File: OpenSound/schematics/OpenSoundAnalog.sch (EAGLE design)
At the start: 68 parts, among them IC1 MCP4822-E/PSOIC8, IC2 QUAD_OPAMPD, IC3 LM317MABT, Q601 BC846, Q701 BC846, Q801 BC846, Q903 BC846, U1 SN74LVC3G17DCTR

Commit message: part routed
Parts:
- added C5: 10u, rcl:CPOL-EUSANYO_SMD_A5
- C2: value 1u -> 10u
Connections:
- net +3V3: no longer C1.1
- net +5V: now also C1.1, C5.+
- net GND: now also C5.-
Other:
- moved on the sheet: C1
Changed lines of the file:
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@@
 <part name="C1" library="resistor" deviceset="C-EU" device="C0603" value="100nF"/>
 <part name="+3V2" library="supply1" deviceset="+3V3" device=""/>
-<part name="+3V3" library="supply1" deviceset="+3V3" device=""/>
 <part name="GND2" library="supply1" deviceset="GND" device=""/>
 <part name="GND3" library="supply1" deviceset="GND" device=""/>
@@
 <part name="P+1" library="supply1" deviceset="+12V" device=""/>
 <part name="P+5" library="supply1" deviceset="+5V" device=""/>
-<part name="C2" library="rcl" deviceset="CPOL-EU" device="SANYO_SMD_A5" value="1u"/>
+<part name="C2" library="rcl" deviceset="CPOL-EU" device="SANYO_SMD_A5" value="10u"/>
 <part name="P+8" library="supply1" deviceset="+5V" device=""/>
 <part name="U1" library="Rebel" deviceset="SN74LVC3G17DCTR" device=""/>
@@
 <part name="R101" library="Rebel" deviceset="R-EU_" device="0603" value="150R"/>
 <part name="C100" library="rcl" deviceset="C-EU" device="C0603" value="100n"/>
+<part name="P+6" library="supply1" deviceset="+5V" device=""/>
+<part name="C5" library="rcl" deviceset="CPOL-EU" device="SANYO_SMD_A5" value="10u"/>
+<part name="P+10" library="supply1" deviceset="+5V" device=""/>
+<part name="GND27" library="supply1" deviceset="GND" device=""/>
 </parts>
 <sheets>
@@
 <instance part="P-7" gate="1" x="157.48" y="30.48"/>
 <instance part="P+2" gate="1" x="157.48" y="50.8"/>
-<instance part="C1" gate="G$1" x="73.66" y="104.14"/>
+<instance part="C1" gate="G$1" x="127" y="-35.56"/>
 <instance part="+3V2" gate="G$1" x="66.04" y="114.3"/>
-<instance part="+3V3" gate="G$1" x="73.66" y="114.3"/>
 <instance part="GND2" gate="1" x="66.04" y="93.98"/>
-<instance part="GND3" gate="1" x="73.66" y="93.98"/>
+<instance part="GND3" gate="1" x="127" y="-45.72"/>
 <instance part="Q903" gate="G$1" x="-19.05" y="97.79"/>
 <instance part="R901" gate="G$1" x="-26.67" y="97.79" rot="MR180"/>
@@
 <instance part="R101" gate="G$1" x="226.06" y="167.64" rot="MR0"/>
 <instance part="C100" gate="G$1" x="223.52" y="154.94" rot="R180"/>
+<instance part="P+6" gate="1" x="127" y="-25.4"/>
+<instance part="C5" gate="G$1" x="55.88" y="104.14"/>
+<instance part="P+10" gate="1" x="55.88" y="114.3"/>
+<instance part="GND27" gate="1" x="55.88" y="93.98"/>
 </instances>
 <busses>
@@
 <pinref part="C1" gate="G$1" pin="2"/>
 <pinref part="GND3" gate="1" pin="GND"/>
-<wire x1="73.66" y1="96.52" x2="73.66" y2="99.06" width="0.1524" layer="91"/>
+<wire x1="127" y1="-43.18" x2="127" y2="-40.64" width="0.1524" layer="91"/>
 </segment>
 <segment>
@@
 <pinref part="C100" gate="G$1" pin="1"/>
 </segment>
+<segment>
+<pinref part="GND27" gate="1" pin="GND"/>
+<pinref part="C5" gate="G$1" pin="-"/>
+<wire x1="55.88" y1="96.52" x2="55.88" y2="99.06" width="0.1524" layer="91"/>
+</segment>
 </net>
 <net name="-12V" class="0">
@@
 <wire x1="101.6" y1="48.26" x2="104.14" y2="48.26" width="0.1524" layer="91"/>
 <wire x1="104.14" y1="48.26" x2="104.14" y2="53.34" width="0.1524" layer="91"/>
+</segment>
+<segment>
+<pinref part="C1" gate="G$1" pin="1"/>
+<wire x1="127" y1="-33.02" x2="127" y2="-27.94" width="0.1524" layer="91"/>
+<pinref part="P+6" gate="1" pin="+5V"/>
+</segment>
+<segment>
+<pinref part="C5" gate="G$1" pin="+"/>
+<pinref part="P+10" gate="1" pin="+5V"/>
+<wire x1="55.88" y1="106.68" x2="55.88" y2="111.76" width="0.1524" layer="91"/>
 </segment>
 </net>
@@
 </segment>
 <segment>
-<pinref part="+3V3" gate="G$1" pin="+3V3"/>
-<pinref part="C1" gate="G$1" pin="1"/>
-<wire x1="73.66" y1="106.68" x2="73.66" y2="111.76" width="0.1524" layer="91"/>
-</segment>
-<segment>

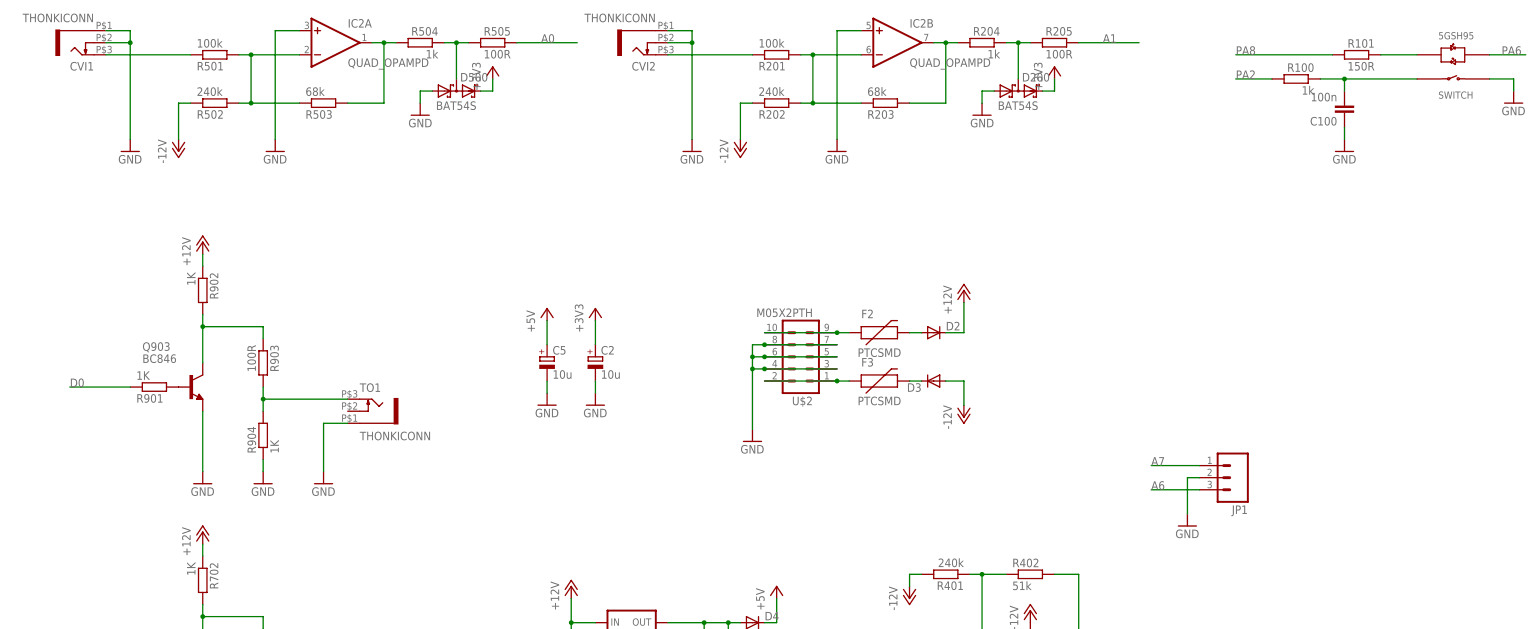
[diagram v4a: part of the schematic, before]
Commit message: connected button and completed routing
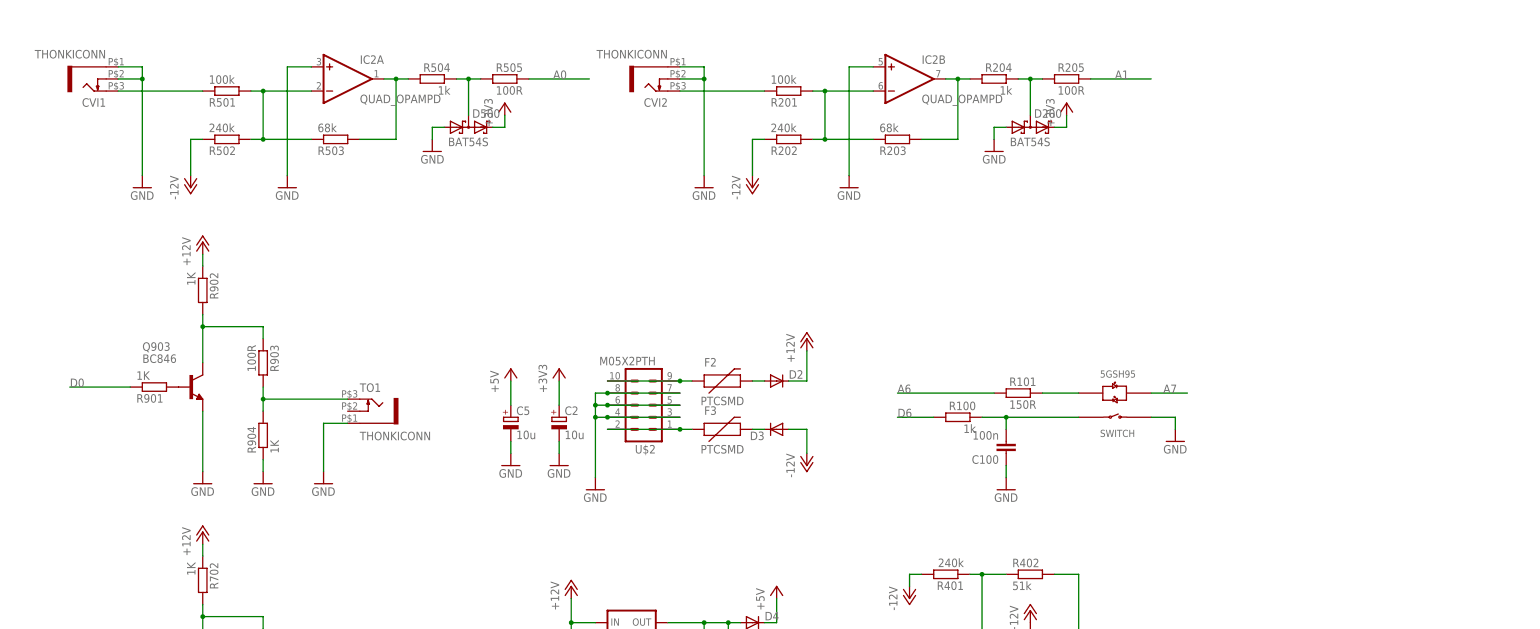
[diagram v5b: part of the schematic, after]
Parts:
- removed JP1: (no value), SparkFun-Connectors:M031X03_NO_SILK
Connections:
- removed net PA2: R100.2
- removed net PA6: U$1.LED_R+
- removed net PA8: R101.2
- net A6: now also R101.2; no longer JP1.3
- net A7: now also U$1.LED_R+; no longer JP1.1
- net D6: now also R100.2
- net GND: no longer JP1.2
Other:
- moved on the sheet: C100, C2, C5, CVI1, CVI2, D2, D200, D3, D500, F2, F3, IC2A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

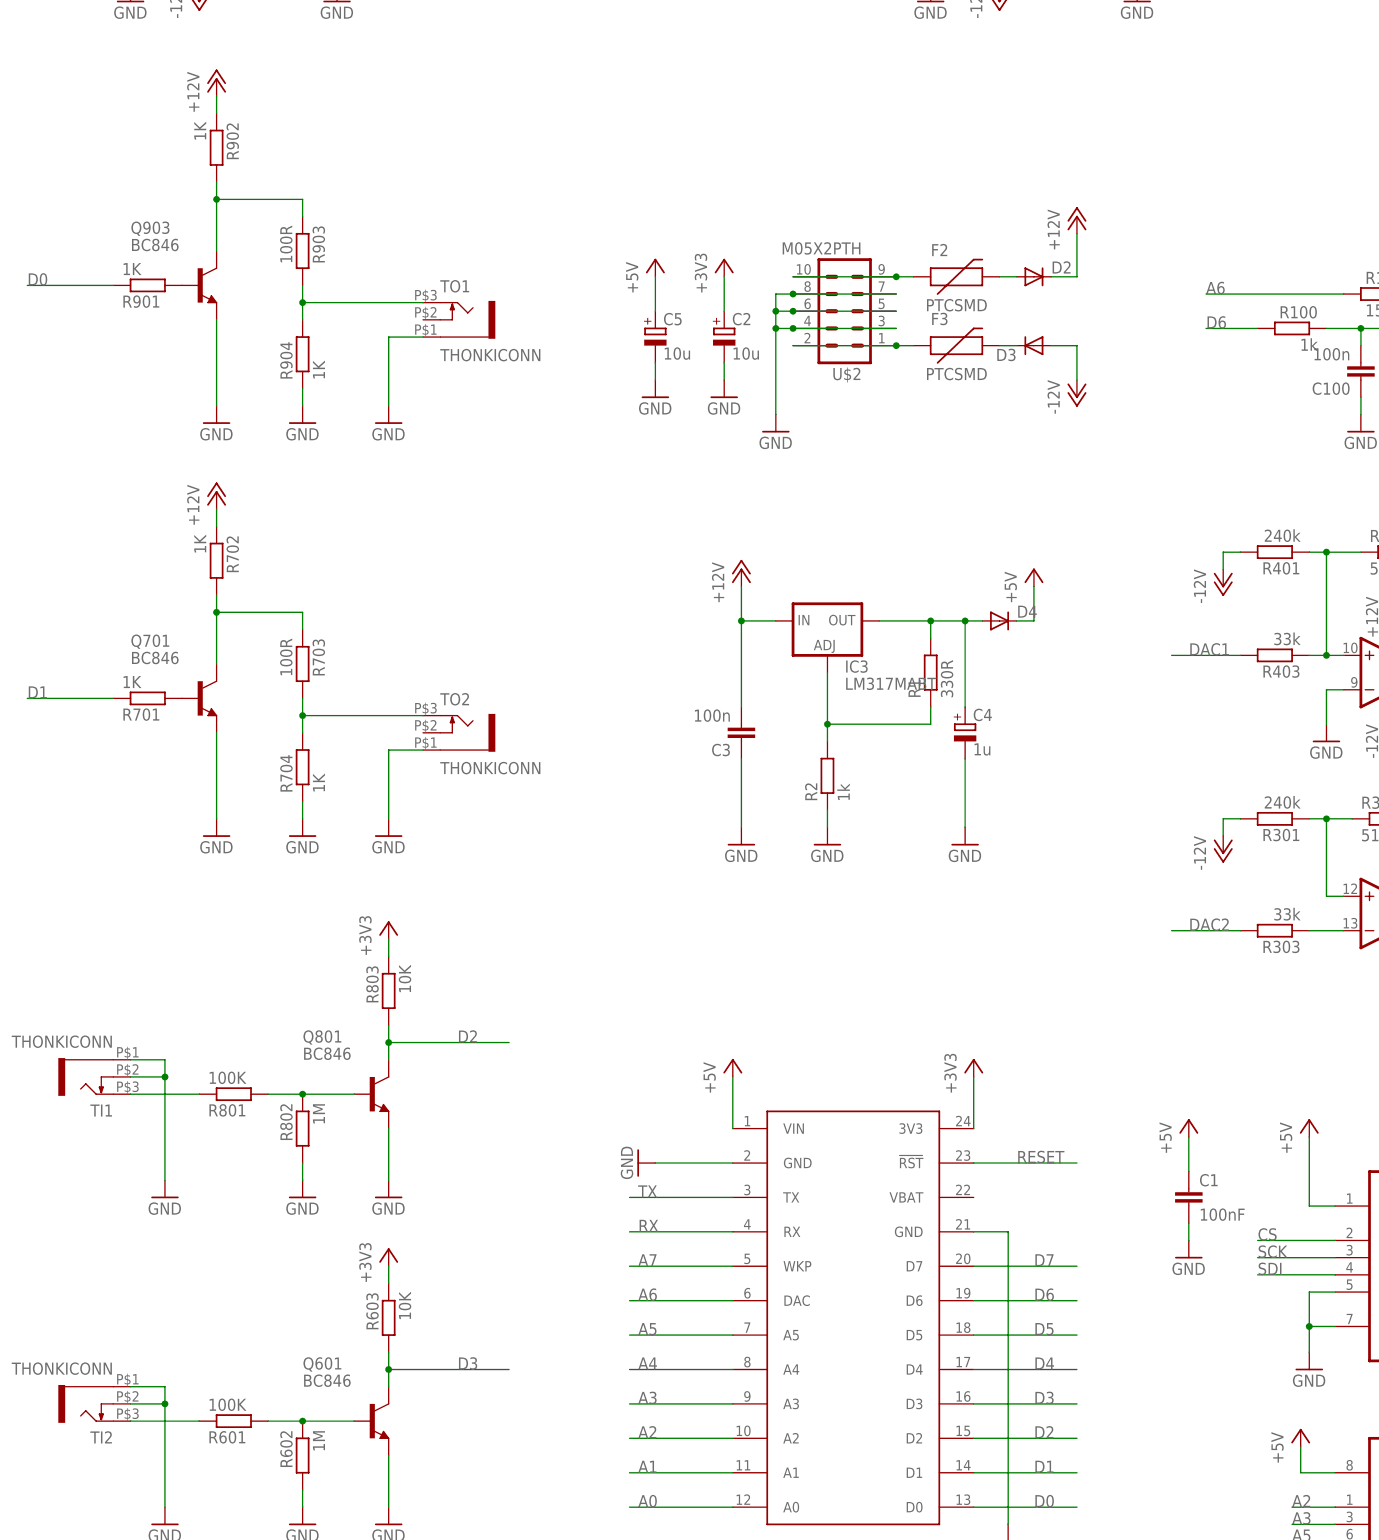
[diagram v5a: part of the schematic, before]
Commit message: changed to uniform value suffixes
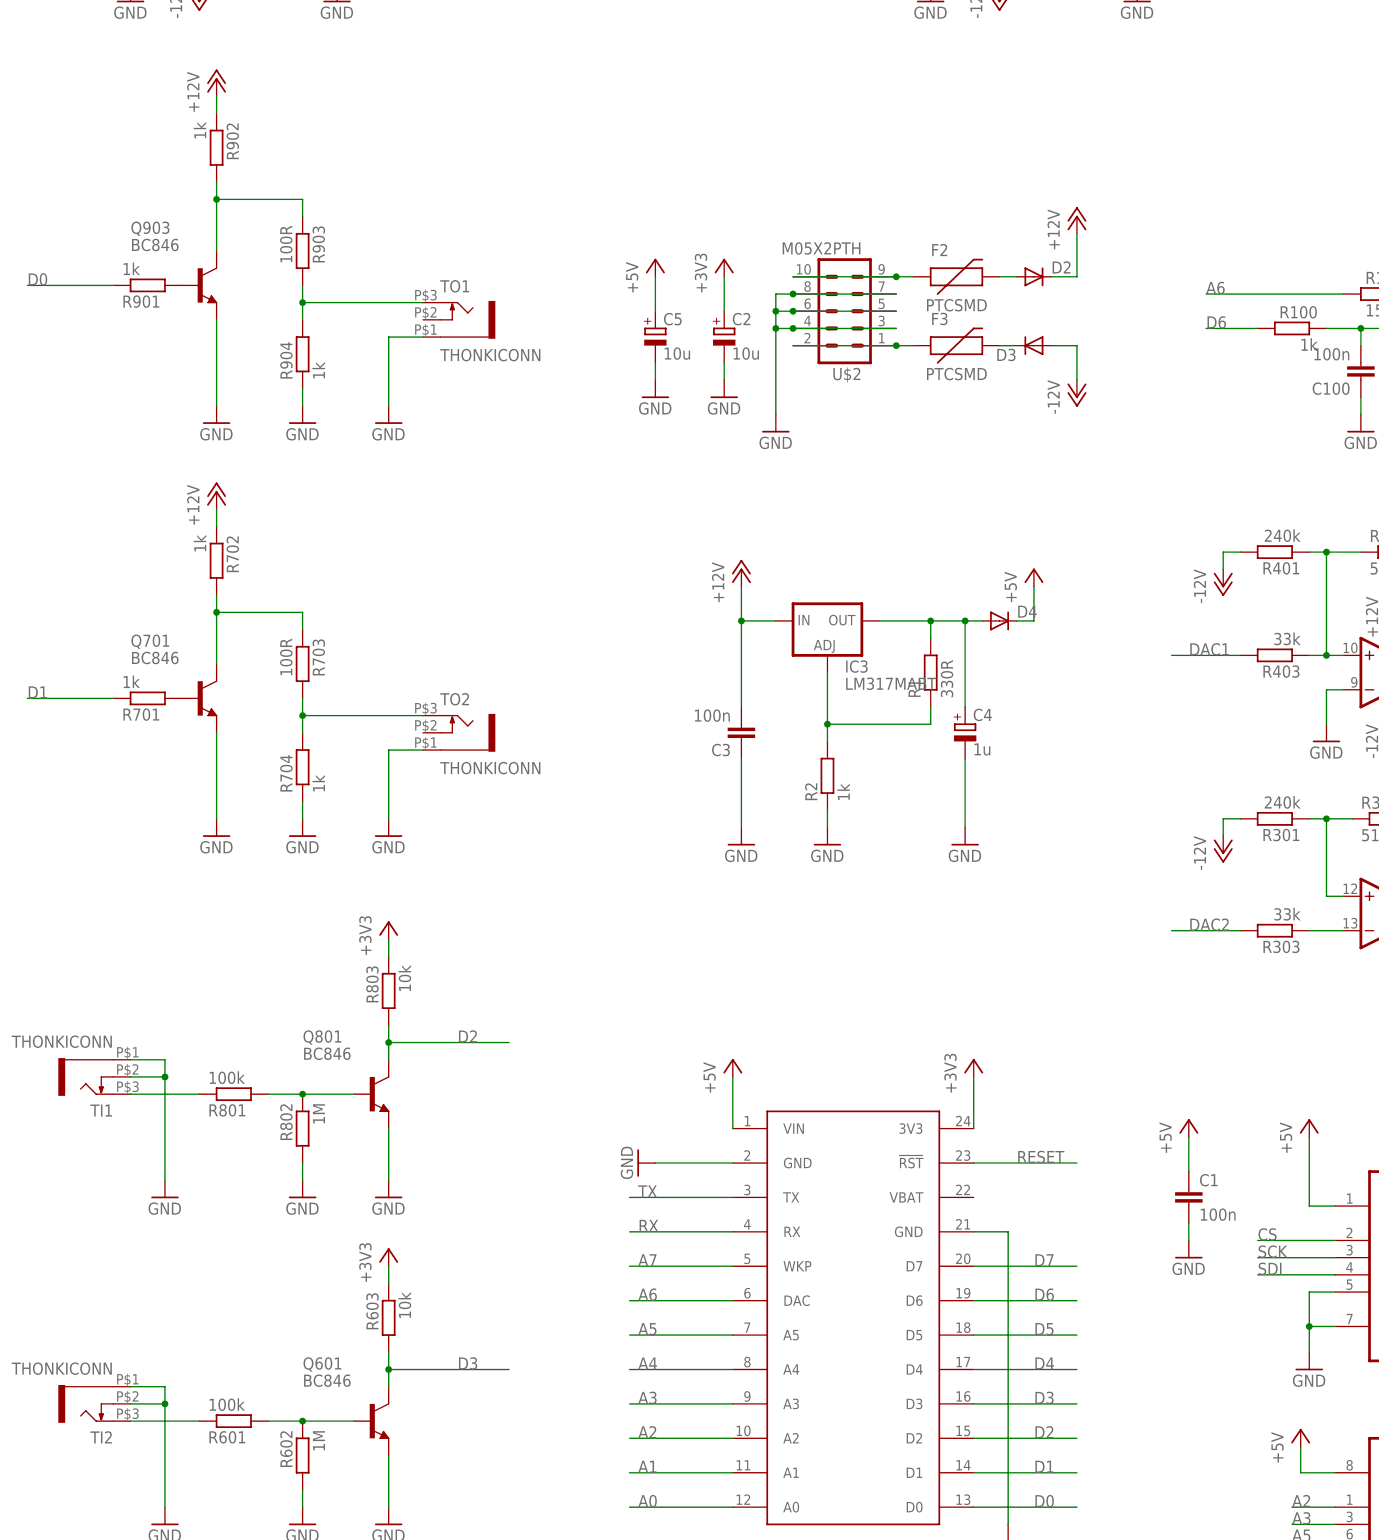
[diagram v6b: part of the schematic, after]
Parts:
- C1: value 100nF -> 100n
- R601, R801: value 100K -> 100k
- R603, R803: value 10K -> 10k
- R701, R702, R704, R901, R902, R904: value 1K -> 1k
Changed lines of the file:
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@@
 </classes>
 <parts>
-<part name="R601" library="Rebel" deviceset="R-EU_" device="0603" value="100K"/>
-<part name="R603" library="Rebel" deviceset="R-EU_" device="0603" value="10K"/>
+<part name="R601" library="Rebel" deviceset="R-EU_" device="0603" value="100k"/>
+<part name="R603" library="Rebel" deviceset="R-EU_" device="0603" value="10k"/>
 <part name="GND12" library="supply1" deviceset="GND" device=""/>
 <part name="Q601" library="transistor" deviceset="BC846" device=""/>
@@
 <part name="+3V14" library="supply1" deviceset="+3V3" device=""/>
 <part name="Q701" library="transistor" deviceset="BC846" device=""/>
-<part name="R701" library="Rebel" deviceset="R-EU_" device="0603" value="1K"/>
+<part name="R701" library="Rebel" deviceset="R-EU_" device="0603" value="1k"/>
 <part name="R703" library="Rebel" deviceset="R-EU_" device="0603" value="100R"/>
-<part name="R704" library="Rebel" deviceset="R-EU_" device="0603" value="1K"/>
+<part name="R704" library="Rebel" deviceset="R-EU_" device="0603" value="1k"/>
 <part name="GND45" library="supply1" deviceset="GND" device=""/>
 <part name="GND46" library="supply1" deviceset="GND" device=""/>
 <part name="GND47" library="supply1" deviceset="GND" device=""/>
-<part name="R702" library="Rebel" deviceset="R-EU_" device="0603" value="1K"/>
+<part name="R702" library="Rebel" deviceset="R-EU_" device="0603" value="1k"/>
 <part name="TO2" library="Rebel" deviceset="THONKICONN" device=""/>
 <part name="P+7" library="supply1" deviceset="+12V" device=""/>
@@
 <part name="P-7" library="supply1" deviceset="-12V" device=""/>
 <part name="P+2" library="supply1" deviceset="+12V" device=""/>
-<part name="C1" library="resistor" deviceset="C-EU" device="C0603" value="100nF"/>
+<part name="C1" library="resistor" deviceset="C-EU" device="C0603" value="100n"/>
 <part name="+3V2" library="supply1" deviceset="+3V3" device=""/>
 <part name="GND2" library="supply1" deviceset="GND" device=""/>
 <part name="GND3" library="supply1" deviceset="GND" device=""/>
 <part name="Q903" library="transistor" deviceset="BC846" device=""/>
-<part name="R901" library="Rebel" deviceset="R-EU_" device="0603" value="1K"/>
+<part name="R901" library="Rebel" deviceset="R-EU_" device="0603" value="1k"/>
 <part name="R903" library="Rebel" deviceset="R-EU_" device="0603" value="100R"/>
-<part name="R904" library="Rebel" deviceset="R-EU_" device="0603" value="1K"/>
+<part name="R904" library="Rebel" deviceset="R-EU_" device="0603" value="1k"/>
 <part name="GND4" library="supply1" deviceset="GND" device=""/>
 <part name="GND5" library="supply1" deviceset="GND" device=""/>
 <part name="GND7" library="supply1" deviceset="GND" device=""/>
-<part name="R902" library="Rebel" deviceset="R-EU_" device="0603" value="1K"/>
+<part name="R902" library="Rebel" deviceset="R-EU_" device="0603" value="1k"/>
 <part name="TO1" library="Rebel" deviceset="THONKICONN" device=""/>
 <part name="P+3" library="supply1" deviceset="+12V" device=""/>
-<part name="R801" library="Rebel" deviceset="R-EU_" device="0603" value="100K"/>
-<part name="R803" library="Rebel" deviceset="R-EU_" device="0603" value="10K"/>
+<part name="R801" library="Rebel" deviceset="R-EU_" device="0603" value="100k"/>
+<part name="R803" library="Rebel" deviceset="R-EU_" device="0603" value="10k"/>
 <part name="GND10" library="supply1" deviceset="GND" device=""/>
 <part name="Q801" library="transistor" deviceset="BC846" device=""/>
